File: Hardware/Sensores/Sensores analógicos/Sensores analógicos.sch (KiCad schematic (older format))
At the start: 3 parts

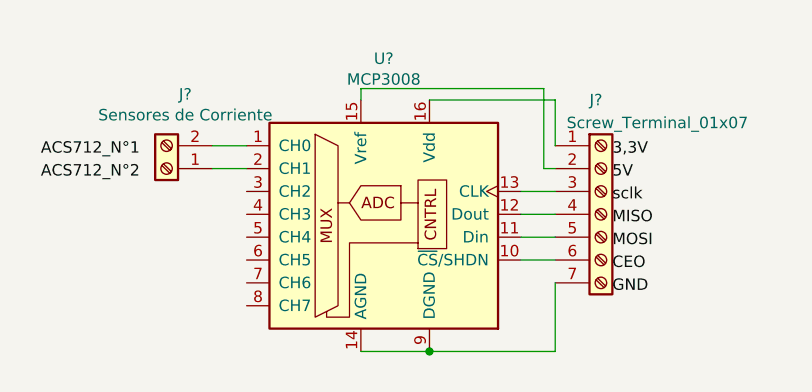
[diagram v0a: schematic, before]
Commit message: PCB de los sensores de corriente
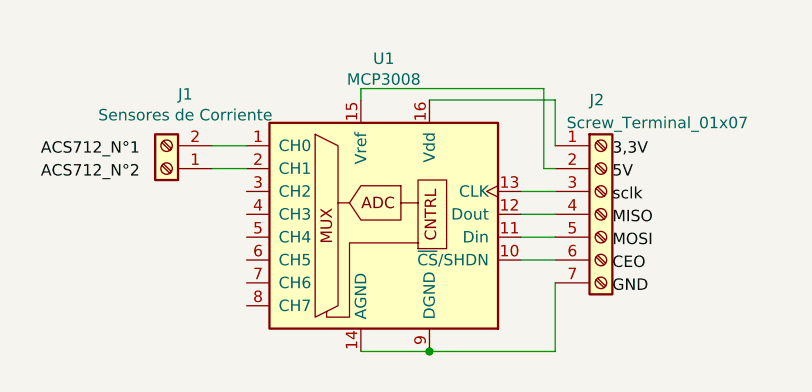
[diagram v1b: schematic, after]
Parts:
- J2: renamed from J?; footprint (none) -> Connector_Molex:Molex_KK-254_AE-6410-07A_1x07_P2.54mm_Vertical
- U1: renamed from U?; footprint (none) -> Package_DIP:DIP-16_W7.62mm
- gave numbers to parts that had none: 1
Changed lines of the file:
@@
 $EndDescr
 $Comp
-L Analog_ADC:MCP3008 U?
+L Analog_ADC:MCP3008 U1
 U 1 1 5EF4E0FD
 P 5500 3050
-F 0 "U?" H 5500 3731 50  0000 C CNN
+F 0 "U1" H 5500 3731 50  0000 C CNN
 F 1 "MCP3008" H 5500 3640 50  0000 C CNN
-F 2 "" H 5600 3150 50  0001 C CNN
+F 2 "Package_DIP:DIP-16_W7.62mm" H 5600 3150 50  0001 C CNN
 F 3 "http://ww1.microchip.com/downloads/en/DeviceDoc/21295d.pdf" H 5600 3150 50  0001 C CNN
 	1    5500 3050
@@
 $EndComp
 $Comp
-L Connector:Screw_Terminal_01x02 J?
+L Connector:Screw_Terminal_01x02 J1
 U 1 1 5EF50EC2
 P 4550 2850
-F 0 "J?" H 4468 2525 50  0000 C CNN
+F 0 "J1" H 4468 2525 50  0000 C CNN
 F 1 "Sensores de Corriente" H 4468 2616 50  0000 C CNN
 F 2 "Connector_Molex:Molex_KK-254_AE-6410-02A_1x02_P2.54mm_Vertical" H 4550 2850 50  0001 C CNN
@@
 	5400 2550 5400 2500
 $Comp
-L Connector:Screw_Terminal_01x07 J?
+L Connector:Screw_Terminal_01x07 J2
 U 1 1 5EF54988
 P 6450 3050
-F 0 "J?" H 6400 3550 50  0000 L CNN
+F 0 "J2" H 6400 3550 50  0000 L CNN
 F 1 "Screw_Terminal_01x07" H 6300 3450 50  0000 L CNN
-F 2 "" H 6450 3050 50  0001 C CNN
+F 2 "Connector_Molex:Molex_KK-254_AE-6410-07A_1x07_P2.54mm_Vertical" H 6450 3050 50  0001 C CNN
 F 3 "~" H 6450 3050 50  0001 C CNN
 	1    6450 3050

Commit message: Esquematico sensor porcentaje de bateria
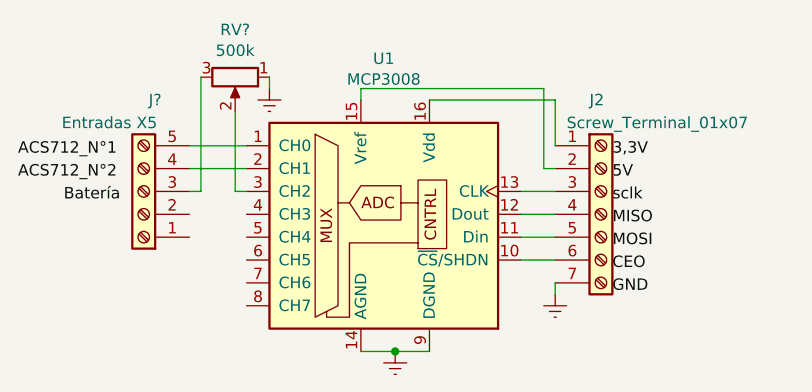
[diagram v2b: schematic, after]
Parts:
- removed J1: Sensores de Corriente, Connector_Molex:Molex_KK-254_AE-6410-02A_1x02_P2.54mm_Vertical, symbol Connector:Screw_Terminal_01x02
- added J?: Entradas X5, Connector_Molex:Molex_KK-254_AE-6410-05A_1x05_P2.54mm_Vertical, symbol Connector:Screw_Terminal_01x05
- added RV?: 500k, Potentiometer_THT:Potentiometer_Bourns_3006P_Horizontal, symbol Device:R_POT
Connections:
- net at U1.1 (CH0): now also J?.5 (Pin_5)
- net Earth: now reaches J2.7 (Pin_7), U1.14 (AGND), U1.9 (DGND)
- net Earth: now also RV?.1
- net at U1.2 (CH1): now also J?.4 (Pin_4)
- net at U1.3 (CH2): now also RV?.2
- new net: J?.3 (Pin_3), RV?.3
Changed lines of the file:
@@
 	1    0    0    -1
 $EndComp
-$Comp
-L Connector:Screw_Terminal_01x02 J1
-U 1 1 5EF50EC2
-P 4550 2850
-F 0 "J1" H 4468 2525 50  0000 C CNN
-F 1 "Sensores de Corriente" H 4468 2616 50  0000 C CNN
-F 2 "Connector_Molex:Molex_KK-254_AE-6410-02A_1x02_P2.54mm_Vertical" H 4550 2850 50  0001 C CNN
-F 3 "~" H 4550 2850 50  0001 C CNN
-	1    4550 2850
-	-1   0    0    1
-$EndComp
-Wire Wire Line
-	4750 2750 4900 2750
-Wire Wire Line
-	4750 2850 4900 2850
-Text Label 4000 2800 0    50   ~ 0
+Text Label 3900 2800 0    50   ~ 0
 ACS712_N°1
-Text Label 4000 2900 0    50   ~ 0
+Text Label 3900 2900 0    50   ~ 0
 ACS712_N°2
-Wire Wire Line
-	5400 3650 5700 3650
 Wire Wire Line
 	5400 2550 5400 2500
@@
 	1    0    0    -1
 $EndComp
-Wire Wire Line
-	5700 3650 6250 3650
-Wire Wire Line
-	6250 3650 6250 3350
-Connection ~ 5700 3650
 Wire Wire Line
 	6100 3250 6250 3250
@@
 Text Label 6500 3400 0    50   ~ 0
 GND
+$Comp
+L Connector:Screw_Terminal_01x05 J?
+U 1 1 5EF696C7
+P 4450 2950
+F 0 "J?" H 4400 2550 50  0000 C CNN
+F 1 "Entradas X5" H 4600 2650 50  0000 C CNN
+F 2 "Connector_Molex:Molex_KK-254_AE-6410-05A_1x05_P2.54mm_Vertical" H 4450 2950 50  0001 C CNN
+F 3 "~" H 4450 2950 50  0001 C CNN
+	1    4450 2950
+	-1   0    0    1
+$EndComp
+$Comp
+L Device:R_POT RV?
+U 1 1 5EF6BB3C
+P 4850 2450
+F 0 "RV?" V 4643 2450 50  0000 C CNN
+F 1 "500k" V 4734 2450 50  0000 C CNN
+F 2 "Potentiometer_THT:Potentiometer_Bourns_3006P_Horizontal" H 4850 2450 50  0001 C CNN
+F 3 "~" H 4850 2450 50  0001 C CNN
+	1    4850 2450
+	0    1    1    0
+$EndComp
+Wire Wire Line
+	4650 2950 4700 2950
+Wire Wire Line
+	4700 2950 4700 2450
+Wire Wire Line
+	4650 2850 4900 2850
+Wire Wire Line
+	4650 2750 4900 2750
+Wire Wire Line
+	4850 2600 4850 2950
+Wire Wire Line
+	4850 2950 4900 2950
+Text Label 4100 3000 0    50   ~ 0
+Batería
+$Comp
+L power:Earth #PWR?
+U 1 1 5EF723B2
+P 5000 2500
+F 0 "#PWR?" H 5000 2250 50  0001 C CNN
+F 1 "Earth" H 5000 2350 50  0001 C CNN
+F 2 "" H 5000 2500 50  0001 C CNN
+F 3 "~" H 5000 2500 50  0001 C CNN
+	1    5000 2500
+	1    0    0    -1
+$EndComp
+Wire Wire Line
+	5000 2450 5000 2500
+$Comp
+L power:Earth #PWR?
+U 1 1 5EF72D32
+P 5550 3650
+F 0 "#PWR?" H 5550 3400 50  0001 C CNN
+F 1 "Earth" H 5550 3500 50  0001 C CNN
+F 2 "" H 5550 3650 50  0001 C CNN
+F 3 "~" H 5550 3650 50  0001 C CNN
+	1    5550 3650
+	1    0    0    -1
+$EndComp
+$Comp
+L power:Earth #PWR?
+U 1 1 5EF73268
+P 6250 3400
+F 0 "#PWR?" H 6250 3150 50  0001 C CNN
+F 1 "Earth" H 6250 3250 50  0001 C CNN
+F 2 "" H 6250 3400 50  0001 C CNN
+F 3 "~" H 6250 3400 50  0001 C CNN
+	1    6250 3400
+	1    0    0    -1
+$EndComp
+Wire Wire Line
+	6250 3350 6250 3400
+Wire Wire Line
+	5700 3650 5550 3650
+Wire Wire Line
+	5400 3650 5550 3650
+Connection ~ 5550 3650
 $EndSCHEMATC

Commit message: PCB Sensor de porcentaje de bateria
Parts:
- gave numbers to parts that had none: 2
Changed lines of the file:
@@
 GND
 $Comp
-L Connector:Screw_Terminal_01x05 J?
+L Connector:Screw_Terminal_01x05 J1
 U 1 1 5EF696C7
 P 4450 2950
-F 0 "J?" H 4400 2550 50  0000 C CNN
+F 0 "J1" H 4400 2550 50  0000 C CNN
 F 1 "Entradas X5" H 4600 2650 50  0000 C CNN
 F 2 "Connector_Molex:Molex_KK-254_AE-6410-05A_1x05_P2.54mm_Vertical" H 4450 2950 50  0001 C CNN
@@
 $EndComp
 $Comp
-L Device:R_POT RV?
+L Device:R_POT RV1
 U 1 1 5EF6BB3C
 P 4850 2450
-F 0 "RV?" V 4643 2450 50  0000 C CNN
+F 0 "RV1" V 4643 2450 50  0000 C CNN
 F 1 "500k" V 4734 2450 50  0000 C CNN
 F 2 "Potentiometer_THT:Potentiometer_Bourns_3006P_Horizontal" H 4850 2450 50  0001 C CNN
@@
 Batería
 $Comp
-L power:Earth #PWR?
+L power:Earth #PWR0101
 U 1 1 5EF723B2
 P 5000 2500
-F 0 "#PWR?" H 5000 2250 50  0001 C CNN
+F 0 "#PWR0101" H 5000 2250 50  0001 C CNN
 F 1 "Earth" H 5000 2350 50  0001 C CNN
 F 2 "" H 5000 2500 50  0001 C CNN
@@
 	5000 2450 5000 2500
 $Comp
-L power:Earth #PWR?
+L power:Earth #PWR0102
 U 1 1 5EF72D32
 P 5550 3650
-F 0 "#PWR?" H 5550 3400 50  0001 C CNN
+F 0 "#PWR0102" H 5550 3400 50  0001 C CNN
 F 1 "Earth" H 5550 3500 50  0001 C CNN
 F 2 "" H 5550 3650 50  0001 C CNN
@@
 $EndComp
 $Comp
-L power:Earth #PWR?
+L power:Earth #PWR0103
 U 1 1 5EF73268
 P 6250 3400
-F 0 "#PWR?" H 6250 3150 50  0001 C CNN
+F 0 "#PWR0103" H 6250 3150 50  0001 C CNN
 F 1 "Earth" H 6250 3250 50  0001 C CNN
 F 2 "" H 6250 3400 50  0001 C CNN
